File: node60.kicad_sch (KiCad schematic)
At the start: 0 parts

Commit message: Schematic capture: power entry (p2) and regulators (p3)
Pages 2 and 3 drawn to the schematic rules adopted on 2026-10-22 (wired
clusters in dashed boxes, labels only between clusters and sheets, one
rail symbol per cluster, every net named, D-45 values with separate
voltage/tolerance/dielectric fields). Design values and their reasons
are on each sheet. Parts not yet in the DropOut library are stock
Device symbols marked PLACEHOLDER with empty MPN fields.

The root index now carries the sheet interfaces as sheet pins, laid out
along the power and signal path. check_schematic.py also fails on
auto-generated net names (rule O-2). CLAUDE.md records the four project
answers and the net-naming decisions.

Co-Authored-By: Claude Opus 5.5 <noreply@anthropic.com>
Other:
- sheet Power entry ports: added BATT_MON, I2C0_TELEMETRY_SCL, I2C0_TELEMETRY_SDA, INH, LM_FLT_L, NTC_RSENSE, TMP175_ALERT_L, VBAT_IN; removed none
- sheet Regulators ports: added INH, RESET_L; removed none
- note added: "Node60 schematic, Architecture Rev A. Page 1 is the index. Sheets are numbered by page; reference designators are page x 100 + nn (R201 = first resistor on page 2). The index is laid out along the power and signal path (D-01/D-02); page numbers follow the Rev A sheet plan. Drawing rules: DropOut handbook chapter 05 (ee-schematic-rules D-rules adopted 2026-10-22). Parts marked PLACEHOLDER (field '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"
- note removed: "Page 1: index. Sheets are numbered by page; reference designators are page x 100 + n (R201 is the first resistor on page 2). Handbook chapter 05."

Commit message: Schematic capture: T1S (p5) and output switch (p6-p8)
Page 5: LAN8670 with per-pin decoupling, RMII mode and PHYAD straps, the
DEC-012 line interface (C0G DC block, ACT1210E-241 choke, VETH100A1DD1
ESD, DNP 100R termination) and the 50 MHz clock feeding PHY and MCU.
Pages 6-8: one TPS2HCS08A-Q1 sheet placed three times, with the SPI
daisy chain, SNS network, VDD filter and package NTC; the root maps
each placement to OUT1..OUT6, SW1..3 and the chain nets.

Co-Authored-By: Claude Opus 5.5 <noreply@anthropic.com>
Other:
- sheet Outputs 1-2 ports: added FLT_L, NTC_SW, OUT_A, OUT_B, SDI, SDO, SNS, SPI1_SWITCH_CS_L, SPI1_SWITCH_SCK; removed none
- sheet Outputs 3-4 ports: added FLT_L, NTC_SW, OUT_A, OUT_B, SDI, SDO, SNS, SPI1_SWITCH_CS_L, SPI1_SWITCH_SCK; removed none
- sheet Outputs 5-6 ports: added FLT_L, NTC_SW, OUT_A, OUT_B, SDI, SDO, SNS, SPI1_SWITCH_CS_L, SPI1_SWITCH_SCK; removed none
- sheet T1S ports: added INH, MDIO0_T1S_MDC, MDIO0_T1S_MDIO, RESET_L, RMII0_T1S_CRS_DV, RMII0_T1S_REF_CLK, RMII0_T1S_RXD0, RMII0_T1S_RXD1, RMII0_T1S_RX_ER, RMII0_T1S_TXD0, RMII0_T1S_TXD1, RMII0_T1S_TX_EN, T1S_IRQ_L, T1S_N, T1S_P; removed none

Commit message: Schematic capture: MCU and NVM (p4), connectors (p9); ERC clean
Page 4: S32K344 in eight boxed units. The supply unit has decoupling per
NXP HDG Rev E2 Table 2; each port unit shows its pin plan and firmware
notes (D-14 as adopted). Pins were checked against NXP's IOMUX table:
EMAC RMII per NXP's TJA1100 use case, LPSPI4 switch chain, LPSPI2 log
flash, LPI2C0 telemetry, ADC1/ADC2 inputs, EIRQ fault lines, SWD and an
LPUART0 debug port. Also the IS25LP032D flash, the Cortex 10-pin header
and the I2C pull-ups.

Page 9: placeholder battery, return, T1S and MX150 output connectors
(all TBD selections), mirrored with pin 1 at the top (D-43), and the
PWR_FLAGs for nets entering the board.

ERC: 0 violations. 17 items are excluded in node60.kicad_pro, each with
its reason (D-52): parallel output pins typed power output in the
library (to be retyped there), and two LAN8670 pins tied to VSS per the
datasheet.

Co-Authored-By: Claude Opus 5.5 <noreply@anthropic.com>
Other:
- sheet Connectors ports: added OUT1, OUT2, OUT3, OUT4, OUT5, OUT6, T1S_N, T1S_P, VBAT_IN; removed none
- sheet MCU and NVM ports: added BATT_MON, I2C0_TELEMETRY_SCL, I2C0_TELEMETRY_SDA, LM_FLT_L, MDIO0_T1S_MDC, MDIO0_T1S_MDIO, NTC_RSENSE, NTC_SW1, NTC_SW2, NTC_SW3, RESET_L, RMII0_T1S_CRS_DV, RMII0_T1S_REF_CLK, RMII0_T1S_RXD0, RMII0_T1S_RXD1, RMII0_T1S_RX_ER, RMII0_T1S_TXD0, RMII0_T1S_TXD1, RMII0_T1S_TX_EN, SPI4_SWITCH_CS_L, SPI4_SWITCH_MISO, SPI4_SWITCH_MOSI, SPI4_SWITCH_SCK, SW1_FLT_L, SW1_SNS, SW2_FLT_L, SW2_SNS, SW3_FLT_L, SW3_SNS, T1S_IRQ_L, TMP175_ALERT_L; removed none
- sheet Outputs 1-2 ports: added SPI4_SWITCH_CS_L, SPI4_SWITCH_SCK; removed SPI1_SWITCH_CS_L, SPI1_SWITCH_SCK
- sheet Outputs 3-4 ports: added SPI4_SWITCH_CS_L, SPI4_SWITCH_SCK; removed SPI1_SWITCH_CS_L, SPI1_SWITCH_SCK
- sheet Outputs 5-6 ports: added SPI4_SWITCH_CS_L, SPI4_SWITCH_SCK; removed SPI1_SWITCH_CS_L, SPI1_SWITCH_SCK

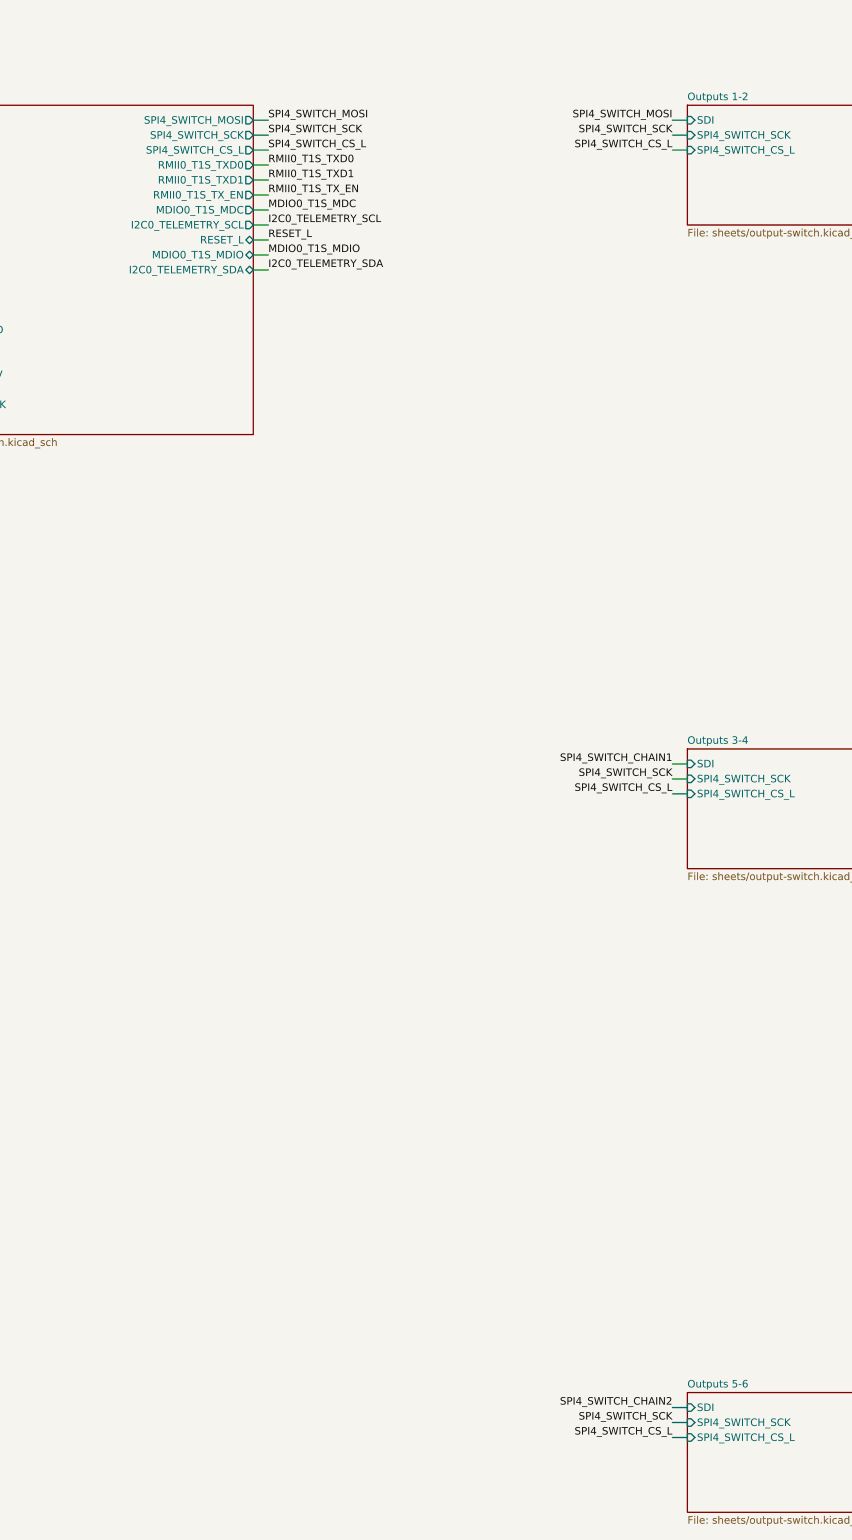
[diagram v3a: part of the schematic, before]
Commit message: Schematic: LHI to the MCU, current notes, net-name map
- LHI on all three TPS2HCS08 is now SW_LHI from S32K344 PTE4 (the
  architecture's GPIO list), still held low by the 10k pull-downs
  through reset.
- Page 4 cites NXP HDG Rev E2 Table 33 for unused GPIO, EXTAL/XTAL and
  the RESET_B pull-up instead of an open 'confirm' note.
- Copper notes for the 10 A output paths (p6) and the 60 A path (p2,
  p9), as IPC-2221 starting estimates to confirm with IPC-2152.
- interfaces.mdx maps the architecture's signal names to the schematic
  nets (RESET_L, T1S_IRQ_L, *_FLT_L, SPI4/SPI2/I2C0 buses).

Co-Authored-By: Claude Opus 5.5 <noreply@anthropic.com>
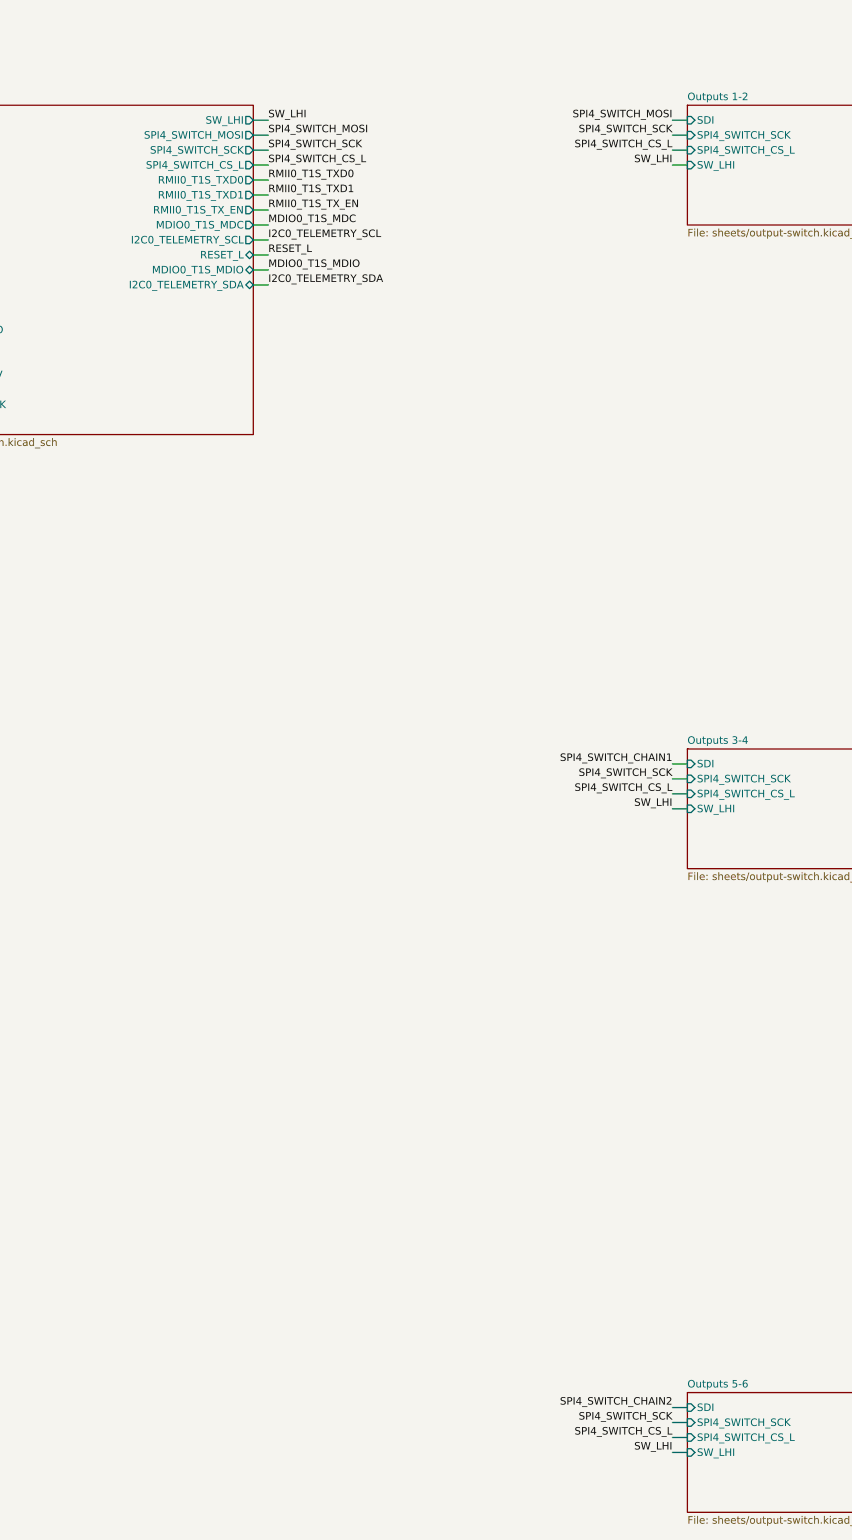
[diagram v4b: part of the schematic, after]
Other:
- sheet MCU and NVM ports: added SW_LHI; removed none
- sheet Outputs 1-2 ports: added SW_LHI; removed none
- sheet Outputs 3-4 ports: added SW_LHI; removed none
- sheet Outputs 5-6 ports: added SW_LHI; removed none
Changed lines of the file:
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@@
 		)
 	)
-	(label "SPI4_SWITCH_MOSI"
+	(label "SW_LHI"
 		(at 373.38 53.34 0)
 		(effects
@@
 		)
 	)
-	(label "SPI4_SWITCH_SCK"
+	(label "SPI4_SWITCH_MOSI"
 		(at 373.38 55.88 0)
 		(effects
@@
 		)
 	)
-	(label "SPI4_SWITCH_CS_L"
+	(label "SPI4_SWITCH_SCK"
 		(at 373.38 58.42 0)
 		(effects
@@
 		)
 	)
-	(label "RMII0_T1S_TXD0"
+	(label "SPI4_SWITCH_CS_L"
 		(at 373.38 60.96 0)
 		(effects
@@
 		)
 	)
-	(label "RMII0_T1S_TXD1"
+	(label "RMII0_T1S_TXD0"
 		(at 373.38 63.5 0)
 		(effects
@@
 		)
 	)
-	(label "RMII0_T1S_TX_EN"
+	(label "RMII0_T1S_TXD1"
 		(at 373.38 66.04 0)
 		(effects
@@
 		)
 	)
-	(label "MDIO0_T1S_MDC"
+	(label "RMII0_T1S_TX_EN"
 		(at 373.38 68.58 0)
 		(effects
@@
 		)
 	)
-	(label "I2C0_TELEMETRY_SCL"
+	(label "MDIO0_T1S_MDC"
 		(at 373.38 71.12 0)
 		(effects
@@
 		)
 	)
-	(label "RESET_L"
+	(label "I2C0_TELEMETRY_SCL"
 		(at 373.38 73.66 0)
 		(effects
@@
 		)
 	)
-	(label "MDIO0_T1S_MDIO"
+	(label "RESET_L"
 		(at 373.38 76.2 0)
 		(effects
@@
 		)
 	)
+	(label "MDIO0_T1S_MDIO"
+		(at 373.38 78.74 0)
+		(effects
+			(font
+				(size 1.27 1.27)
+			)
+			(justify left bottom)
+		)
+	)
+	(wire
+		(pts
+			(xy 370.84 81.28)
+			(xy 373.38 81.28)
+		)
+		(stroke
+			(width 0)
+			(type default)
+		)
+	)
 	(label "I2C0_TELEMETRY_SDA"
-		(at 373.38 78.74 0)
+		(at 373.38 81.28 0)
 		(effects
 			(font
@@
 			)
 		)
+		(pin "SW_LHI" output
+			(at 370.84 53.34 0)
+			(effects
+				(font
+					(size 1.27 1.27)
+				)
+				(justify right)
+			)
+		)
 		(pin "SPI4_SWITCH_MOSI" output
-			(at 370.84 53.34 0)
+			(at 370.84 55.88 0)
 			(effects
 				(font
@@
 		)
 		(pin "SPI4_SWITCH_SCK" output
-			(at 370.84 55.88 0)
+			(at 370.84 58.42 0)
 			(effects
 				(font
@@
 		)
 		(pin "SPI4_SWITCH_CS_L" output
-			(at 370.84 58.42 0)
+			(at 370.84 60.96 0)
 			(effects
 				(font
@@
 		)
 		(pin "RMII0_T1S_TXD0" output
-			(at 370.84 60.96 0)
+			(at 370.84 63.5 0)
 			(effects
 				(font
@@
 		)
 		(pin "RMII0_T1S_TXD1" output
-			(at 370.84 63.5 0)
+			(at 370.84 66.04 0)
 			(effects
 				(font
@@
 		)
 		(pin "RMII0_T1S_TX_EN" output
-			(at 370.84 66.04 0)
+			(at 370.84 68.58 0)
 			(effects
 				(font
@@
 		)
 		(pin "MDIO0_T1S_MDC" output
-			(at 370.84 68.58 0)
+			(at 370.84 71.12 0)
 			(effects
 				(font
@@
 		)
 		(pin "I2C0_TELEMETRY_SCL" output
-			(at 370.84 71.12 0)
+			(at 370.84 73.66 0)
 			(effects
 				(font
@@
 		)
 		(pin "RESET_L" bidirectional
-			(at 370.84 73.66 0)
+			(at 370.84 76.2 0)
 			(effects
 				(font
@@
 		)
 		(pin "MDIO0_T1S_MDIO" bidirectional
-			(at 370.84 76.2 0)
+			(at 370.84 78.74 0)
 			(effects
 				(font
@@
 		)
 		(pin "I2C0_TELEMETRY_SDA" bidirectional
-			(at 370.84 78.74 0)
+			(at 370.84 81.28 0)
 			(effects
 				(font
@@
 	(wire
 		(pts
+			(xy 444.5 60.96)
+			(xy 441.96 60.96)
+		)
+		(stroke
+			(width 0)
+			(type default)
+		)
+	)
+	(label "SW_LHI"
+		(at 441.96 60.96 180)
+		(effects
+			(font
+				(size 1.27 1.27)
+			)
+			(justify right bottom)
+		)
+	)
+	(wire
+		(pts
 			(xy 505.46 53.34)
 			(xy 508 53.34)
@@
 			)
 		)
+		(pin "SW_LHI" input
+			(at 444.5 60.96 180)
+			(effects
+				(font
+					(size 1.27 1.27)
+				)
+				(justify left)
+			)
+		)
 		(pin "SDO" output
 			(at 505.46 53.34 0)
@@
 	(label "SPI4_SWITCH_CS_L"
 		(at 441.96 167.64 180)
+		(effects
+			(font
+				(size 1.27 1.27)
+			)
+			(justify right bottom)
+		)
+	)
+	(wire
+		(pts
+			(xy 444.5 170.18)
+			(xy 441.96 170.18)
+		)
+		(stroke
+			(width 0)
+			(type default)
+		)
+	)
+	(label "SW_LHI"
+		(at 441.96 170.18 180)
 		(effects
 			(font
@@
 			)
 		)
+		(pin "SW_LHI" input
+			(at 444.5 170.18 180)
+			(effects
+				(font
+					(size 1.27 1.27)
+				)
+				(justify left)
+			)
+		)
 		(pin "SDO" output
 			(at 505.46 162.56 0)
@@
 	(label "SPI4_SWITCH_CS_L"
 		(at 441.96 276.86 180)
+		(effects
+			(font
+				(size 1.27 1.27)
+			)
+			(justify right bottom)
+		)
+	)
+	(wire
+		(pts
+			(xy 444.5 279.4)
+			(xy 441.96 279.4)
+		)
+		(stroke
+			(width 0)
+			(type default)
+		)
+	)
+	(label "SW_LHI"
+		(at 441.96 279.4 180)
 		(effects
 			(font
@@
 			(effects
 				(font
+					(size 1.27 1.27)
+				)
+				(justify left)
+			)
+		)
+		(pin "SW_LHI" input
+			(at 444.5 279.4 180)
+			(effects
+				(font

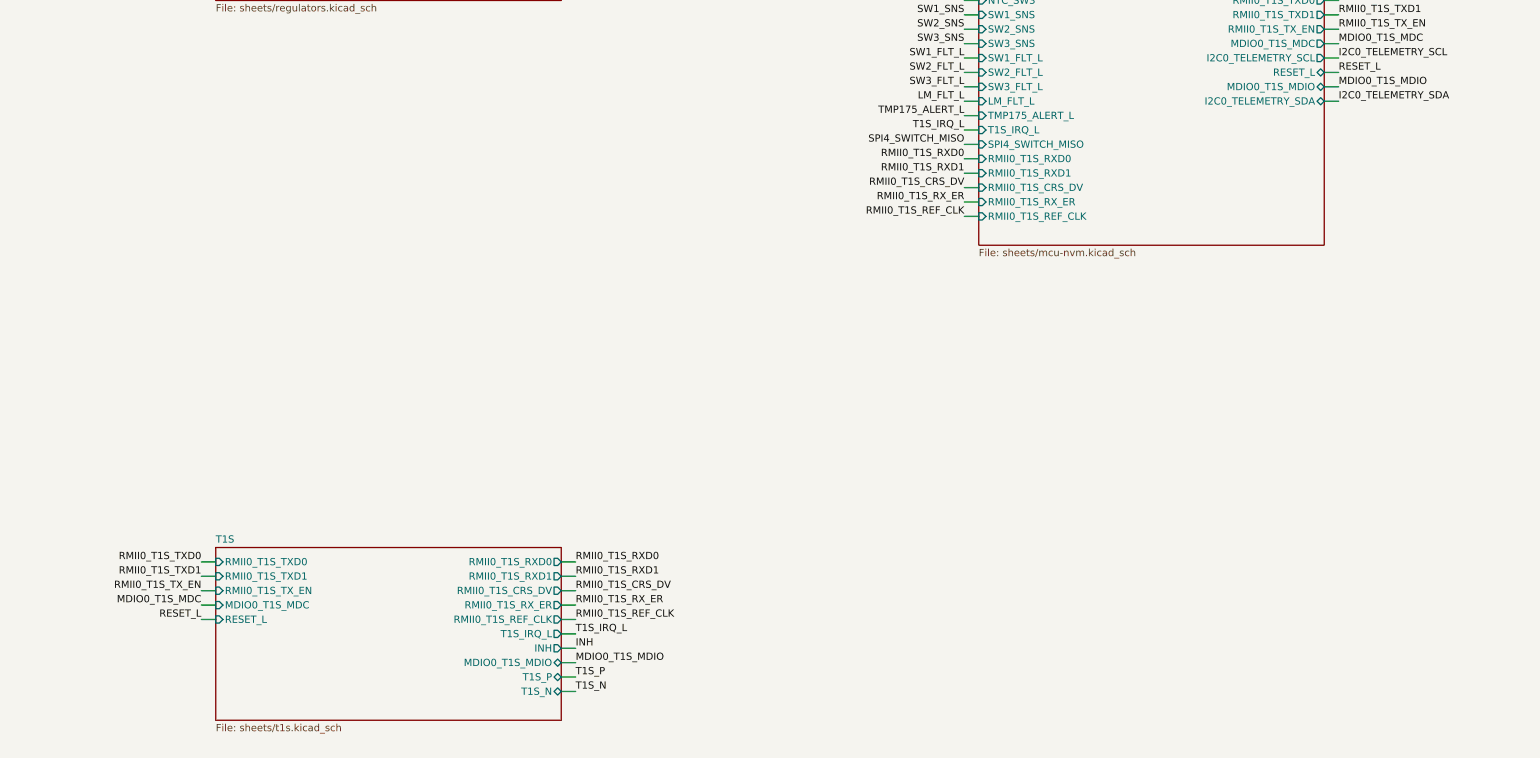
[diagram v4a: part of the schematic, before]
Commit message: DEC-017: T1S bus pass-through and relay-switched termination
The user asked for a second T1S connector so a downstream node can join
the bus, and a termination that can be switched between bus end and
mid-bus (2026-10-28).

- p9: J912, a second ATM13-2P-BM04 in parallel with J903
- p5: R502 (single 100R, not fitted) replaced by the OPEN Alliance
  split termination: latching relay K501 (Omron G6KU-2F-Y-T1-TRS DC3,
  +125 °C) selects 49.9R (end, SET) or 1.5k (drop, RESET) legs to a
  centre tap with 100nF || 100k; Q501/Q502 (DMC2710UVQ-7) half-bridges
  drive the coil from 3V3_MAIN
- p4/root: PTD0 -> T1S_TERM_END, PTD1 -> T1S_TERM_DROP
- Library pinned to dropout-kicad-library PR #37 head db07592; the new
  DropOut_Relay / DropOut_Relay_SMD libraries are in the library tables
- DEC-017, parts, GATE-NET-02 (switched termination), GATE-NET-01 wake
  test in both states, firmware and network pages, GATE-MCU-01 addendum

Co-Authored-By: Claude Opus 5.5 <noreply@anthropic.com>
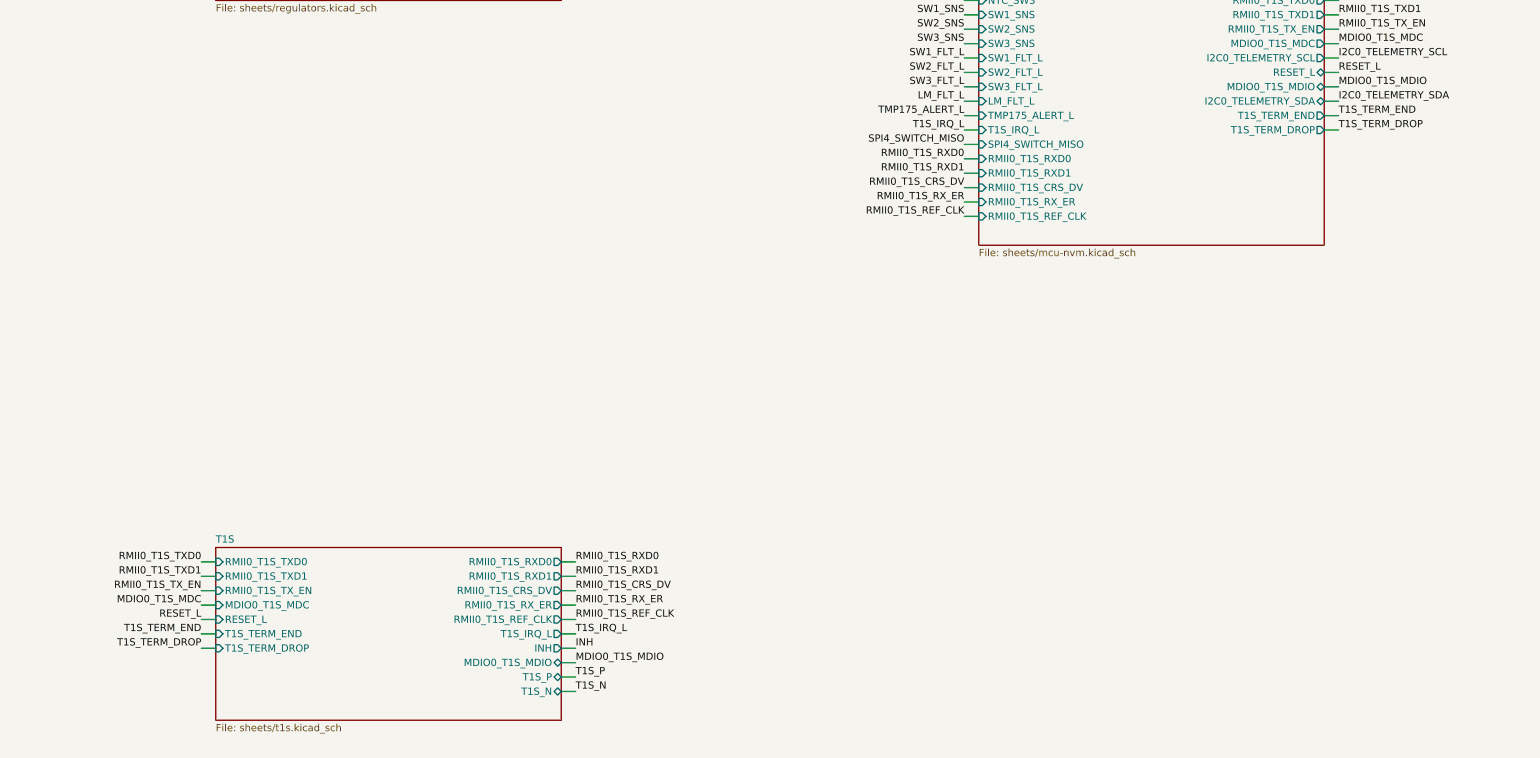
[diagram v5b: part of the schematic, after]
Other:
- sheet MCU and NVM ports: added T1S_TERM_DROP, T1S_TERM_END; removed none
- sheet T1S ports: added T1S_TERM_DROP, T1S_TERM_END; removed none
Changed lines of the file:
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@@
+			)
+		)
+		(pin "T1S_TERM_END" output
+			(at 370.84 83.82 0)
+			(effects
+				(font
+					(size 1.27 1.27)
+				)
+				(justify right)
+			)
+		)
+		(pin "T1S_TERM_DROP" output
+			(at 370.84 86.36 0)
+			(effects
+				(font
+					(size 1.27 1.27)
+				)
+				(justify right)
 			)
 		)
@@
 			)
 		)
+		(pin "T1S_TERM_END" input
+			(at 175.26 175.26 180)
+			(effects
+				(font
+					(size 1.27 1.27)
+				)
+				(justify left)
+			)
+		)
+		(pin "T1S_TERM_DROP" input
+			(at 175.26 177.8 180)
+			(effects
+				(font
+					(size 1.27 1.27)
+				)
+				(justify left)
+			)
+		)
 		(instances
 			(project "node60"
@@
 		)
 	)
+	(wire
+		(pts
+			(xy 370.84 83.82)
+			(xy 373.38 83.82)
+		)
+		(stroke
+			(width 0)
+			(type default)
+		)
+	)
+	(label "T1S_TERM_END"
+		(at 373.38 83.82 0)
+		(effects
+			(font
+				(size 1.27 1.27)
+			)
+			(justify left bottom)
+		)
+	)
+	(wire
+		(pts
+			(xy 370.84 86.36)
+			(xy 373.38 86.36)
+		)
+		(stroke
+			(width 0)
+			(type default)
+		)
+	)
+	(label "T1S_TERM_DROP"
+		(at 373.38 86.36 0)
+		(effects
+			(font
+				(size 1.27 1.27)
+			)
+			(justify left bottom)
+		)
+	)
+	(wire
+		(pts
+			(xy 175.26 175.26)
+			(xy 172.72 175.26)
+		)
+		(stroke
+			(width 0)
+			(type default)
+		)
+	)
+	(label "T1S_TERM_END"
+		(at 172.72 175.26 180)
+		(effects
+			(font
+				(size 1.27 1.27)
+			)
+			(justify right bottom)
+		)
+	)
+	(wire
+		(pts
+			(xy 175.26 177.8)
+			(xy 172.72 177.8)
+		)
+		(stroke
+			(width 0)
+			(type default)
+		)
+	)
+	(label "T1S_TERM_DROP"
+		(at 172.72 177.8 180)
+		(effects
+			(font
+				(size 1.27 1.27)
+			)
+			(justify right bottom)
+		)
+	)
